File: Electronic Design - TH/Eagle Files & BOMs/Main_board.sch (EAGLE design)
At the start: 46 parts, among them IC2 ATMEGA328-PU, Q1 BSS192P, Q2 FQD7P20, X1 16MHz

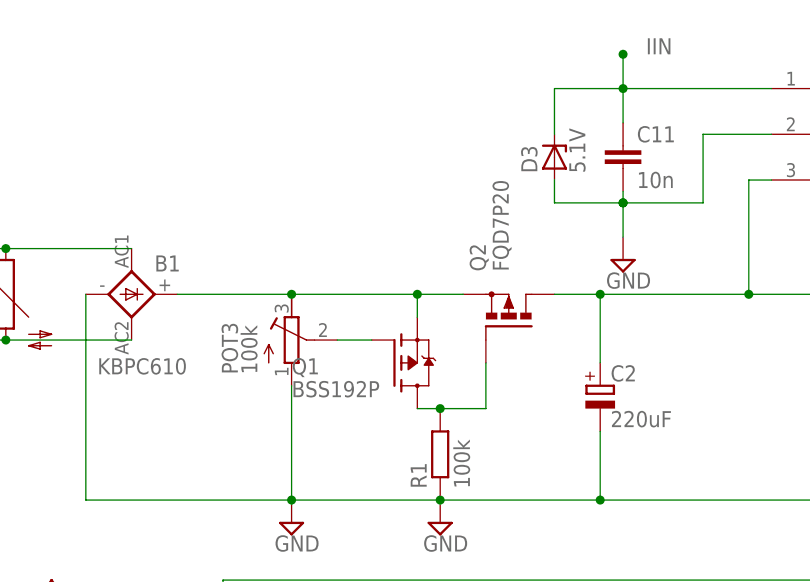
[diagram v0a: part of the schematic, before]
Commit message: replaced SMD resistors, caps and MOSFETs with TH components
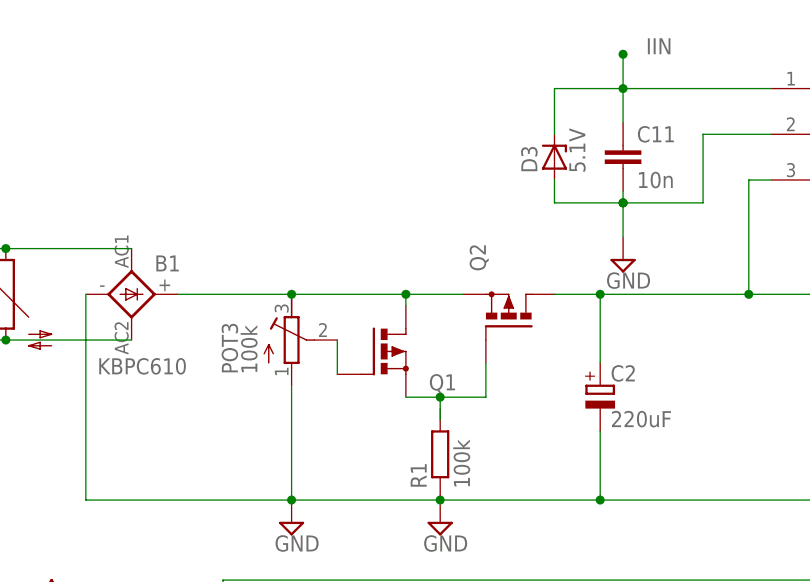
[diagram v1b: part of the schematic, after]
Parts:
- C1, C10, C11, C4, C5, C6, C7: device resistor:C-EUC1206K -> resistor:C-EU050-024X044
- C8, C9: device resistor:C-EUC0805K -> resistor:C-EU050-024X044
- PWR, UC_PWR: device adafruit:LEDSMT1206 -> led:LED3MM
- Q1: value BSS192P -> (none); device Samson:BSS192P -> Samson:PMOSFET_PTO220BH
- Q2: value FQD7P20 -> (none); device Samson:FQD7P20 -> Samson:PMOSFET_PTO220BH
- R10, R9: device resistor:R-EU_R0805 -> resistor:R-EU_0207/10
- R11, R12, R4, R5, R7, R8: device resistor:R-EU_R1206 -> resistor:R-EU_0207/10
- R2: device resistor:R-EU_M1206 -> resistor:R-EU_0207/15
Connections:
- net Q2_GATE: now also Q1.S; no longer Q1.D, R1.2
- net VIN_UNPROTECTED: now also Q1.D; no longer Q1.S
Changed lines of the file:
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@@
 <parts>
 <part name="B1" library="rectifier" deviceset="GBPC6" device="" value="KBPC610"/>
-<part name="C1" library="resistor" deviceset="C-EU" device="C1206K" value="10n"/>
+<part name="C1" library="resistor" deviceset="C-EU" device="050-024X044" value="10n"/>
 <part name="C2" library="resistor" deviceset="CPOL-EU" device="E3.5-10" value="220uF"/>
 <part name="POT3" library="resistor" deviceset="R-TRIMM" device="3296W" value="100k"/>
@@
 <part name="IC2" library="Arduino-AVR" deviceset="ATMEGA168-PU" device="" value="ATMEGA328-PU"/>
 <part name="X1" library="crystal" deviceset="CRYSTAL" device="HC49S" value="16MHz"/>
-<part name="R4" library="resistor" deviceset="R-EU_" device="R1206" value="10k"/>
+<part name="R4" library="resistor" deviceset="R-EU_" device="0207/10" value="10k"/>
 <part name="+5V1" library="supply1" deviceset="+5V" device=""/>
-<part name="C7" library="resistor" deviceset="C-EU" device="C1206K" value="0.1u"/>
-<part name="C9" library="resistor" deviceset="C-EU" device="C0805K" value="22p"/>
-<part name="C8" library="resistor" deviceset="C-EU" device="C0805K" value="22p"/>
+<part name="C7" library="resistor" deviceset="C-EU" device="050-024X044" value="0.1u"/>
+<part name="C9" library="resistor" deviceset="C-EU" device="050-024X044" value="22p"/>
+<part name="C8" library="resistor" deviceset="C-EU" device="050-024X044" value="22p"/>
 <part name="SUPPLY14" library="supply2" deviceset="GND" device=""/>
 <part name="SUPPLY17" library="supply2" deviceset="GND" device=""/>
@@
 <part name="S2" library="switch-omron" deviceset="10-XX" device=""/>
 <part name="+5V2" library="supply1" deviceset="+5V" device=""/>
-<part name="R5" library="resistor" deviceset="R-EU_" device="R1206" value="10k"/>
+<part name="R5" library="resistor" deviceset="R-EU_" device="0207/10" value="10k"/>
 <part name="SUPPLY3" library="supply2" deviceset="GND" device=""/>
 <part name="+5V3" library="supply1" deviceset="+5V" device=""/>
@@
 <part name="+3V1" library="supply1" deviceset="+5V" device=""/>
 <part name="VOUT" library="pinhead" deviceset="PINHD-1X3" device=""/>
-<part name="C6" library="resistor" deviceset="C-EU" device="C1206K" value="0.1u"/>
-<part name="C10" library="resistor" deviceset="C-EU" device="C1206K" value="0.1u"/>
+<part name="C6" library="resistor" deviceset="C-EU" device="050-024X044" value="0.1u"/>
+<part name="C10" library="resistor" deviceset="C-EU" device="050-024X044" value="0.1u"/>
 <part name="AIO" library="pinhead" deviceset="PINHD-1X6" device=""/>
 <part name="+5V4" library="supply1" deviceset="+5V" device=""/>
-<part name="R2" library="resistor" deviceset="R-EU_" device="M1206" value="0R01"/>
+<part name="R2" library="resistor" deviceset="R-EU_" device="0207/15" value="0R01"/>
 <part name="+3V2" library="supply1" deviceset="+5V" device=""/>
 <part name="SUPPLY1" library="supply2" deviceset="GND" device=""/>
 <part name="SUPPLY8" library="supply2" deviceset="GND" device=""/>
-<part name="R7" library="resistor" deviceset="R-EU_" device="R1206" value="1k"/>
-<part name="R8" library="resistor" deviceset="R-EU_" device="R1206" value="3k"/>
+<part name="R7" library="resistor" deviceset="R-EU_" device="0207/10" value="1k"/>
+<part name="R8" library="resistor" deviceset="R-EU_" device="0207/10" value="3k"/>
 <part name="U$1" library="Samson" deviceset="LM317" device=""/>
 <part name="U$2" library="Samson" deviceset="CS30" device=""/>
-<part name="C4" library="resistor" deviceset="C-EU" device="C1206K" value="0.1u"/>
-<part name="C5" library="resistor" deviceset="C-EU" device="C1206K" value="0.1u"/>
+<part name="C4" library="resistor" deviceset="C-EU" device="050-024X044" value="0.1u"/>
+<part name="C5" library="resistor" deviceset="C-EU" device="050-024X044" value="0.1u"/>
 <part name="SUPPLY10" library="supply2" deviceset="GND" device=""/>
 <part name="SUPPLY11" library="supply2" deviceset="GND" device=""/>
-<part name="C11" library="resistor" deviceset="C-EU" device="C1206K" value="10n"/>
+<part name="C11" library="resistor" deviceset="C-EU" device="050-024X044" value="10n"/>
 <part name="D3" library="diode" deviceset="ZPD" device="" value="5.1V"/>
-<part name="R9" library="resistor" deviceset="R-EU_" device="R0805" value="21k5"/>
-<part name="R10" library="resistor" deviceset="R-EU_" device="R0805" value="1k13"/>
+<part name="R9" library="resistor" deviceset="R-EU_" device="0207/10" value="21k5"/>
+<part name="R10" library="resistor" deviceset="R-EU_" device="0207/10" value="1k13"/>
 <part name="SUPPLY12" library="supply2" deviceset="GND" device=""/>
 <part name="D4" library="diode" deviceset="ZPD" device="" value="5.1V"/>
 <part name="SUPPLY13" library="supply2" deviceset="GND" device=""/>
 <part name="D5" library="diode" deviceset="ZPD" device="" value="5.1V"/>
-<part name="UC_PWR" library="adafruit" deviceset="LED" device="SMT1206"/>
-<part name="PWR" library="adafruit" deviceset="LED" device="SMT1206"/>
-<part name="R11" library="resistor" deviceset="R-EU_" device="R1206" value="2k"/>
-<part name="R12" library="resistor" deviceset="R-EU_" device="R1206" value="2k"/>
+<part name="UC_PWR" library="led" deviceset="LED" device="3MM"/>
+<part name="PWR" library="led" deviceset="LED" device="3MM"/>
+<part name="R11" library="resistor" deviceset="R-EU_" device="0207/10" value="2k"/>
+<part name="R12" library="resistor" deviceset="R-EU_" device="0207/10" value="2k"/>
 <part name="SUPPLY15" library="supply2" deviceset="GND" device=""/>
-<part name="Q1" library="Samson" deviceset="BSS192P" device=""/>
-<part name="Q2" library="Samson" deviceset="FQD7P20" device=""/>
+<part name="Q1" library="Samson" deviceset="PMOSFET_P" device="TO220BH"/>
+<part name="Q2" library="Samson" deviceset="PMOSFET_P" device="TO220BH"/>
 <part name="F2" library="fuse" deviceset="FUSE" device="SH22,5A" value="FUSESH22,5A"/>
 <part name="C12" library="resistor" deviceset="CPOL-EU" device="E3.5-8" value="100uF"/>
@@
 <instance part="R12" gate="G$1" x="138.43" y="33.02" rot="R90"/>
 <instance part="SUPPLY15" gate="GND" x="138.43" y="24.13"/>
-<instance part="Q1" gate="G$1" x="-52.07" y="81.28" rot="MR180"/>
+<instance part="Q1" gate="G$1" x="-55.88" y="82.55" rot="MR180"/>
 <instance part="Q2" gate="G$1" x="-41.91" y="86.36" rot="R90"/>
 <instance part="F2" gate="G$1" x="-111.76" y="93.98" smashed="yes">
@@
 <net name="VIN_UNPROTECTED" class="0">
 <segment>
-<wire x1="-52.07" y1="86.36" x2="-52.07" y2="88.9" width="0.1524" layer="91"/>
-<wire x1="-52.07" y1="88.9" x2="-46.99" y2="88.9" width="0.1524" layer="91"/>
 <pinref part="POT3" gate="G$1" pin="E"/>
-<wire x1="-66.04" y1="88.9" x2="-52.07" y2="88.9" width="0.1524" layer="91"/>
-<junction x="-52.07" y="88.9"/>
+<wire x1="-66.04" y1="88.9" x2="-53.34" y2="88.9" width="0.1524" layer="91"/>
 <pinref part="B1" gate="1" pin="+"/>
+<wire x1="-53.34" y1="88.9" x2="-46.99" y2="88.9" width="0.1524" layer="91"/>
 <wire x1="-78.74" y1="88.9" x2="-66.04" y2="88.9" width="0.1524" layer="91"/>
 <junction x="-66.04" y="88.9"/>
+<pinref part="Q2" gate="G$1" pin="S"/>
+<pinref part="Q1" gate="G$1" pin="D"/>
+<wire x1="-53.34" y1="87.63" x2="-53.34" y2="88.9" width="0.1524" layer="91"/>
+<junction x="-53.34" y="88.9"/>
+</segment>
+</net>
+<net name="Q2_GATE" class="0">
+<segment>
+<pinref part="Q2" gate="G$1" pin="G"/>
 <pinref part="Q1" gate="G$1" pin="S"/>
-<pinref part="Q2" gate="G$1" pin="S"/>
-</segment>
-</net>
-<net name="Q2_GATE" class="0">
-<segment>
-<pinref part="R1" gate="G$1" pin="2"/>
-<wire x1="-52.07" y1="76.2" x2="-49.53" y2="76.2" width="0.1524" layer="91"/>
-<wire x1="-49.53" y1="76.2" x2="-44.45" y2="76.2" width="0.1524" layer="91"/>
-<wire x1="-44.45" y1="76.2" x2="-44.45" y2="81.28" width="0.1524" layer="91"/>
-<junction x="-49.53" y="76.2"/>
-<pinref part="Q1" gate="G$1" pin="D"/>
-<pinref part="Q2" gate="G$1" pin="G"/>
+<wire x1="-44.45" y1="77.47" x2="-44.45" y2="81.28" width="0.1524" layer="91"/>
+<wire x1="-53.34" y1="77.47" x2="-49.53" y2="77.47" width="0.1524" layer="91"/>
+<wire x1="-49.53" y1="74.93" x2="-49.53" y2="77.47" width="0.1524" layer="91"/>
+<wire x1="-49.53" y1="77.47" x2="-44.45" y2="77.47" width="0.1524" layer="91"/>
+<junction x="-49.53" y="77.47"/>
 </segment>
 </net>
@@
 <segment>
 <pinref part="POT3" gate="G$1" pin="S"/>
-<wire x1="-57.15" y1="83.82" x2="-60.96" y2="83.82" width="0.1524" layer="91"/>
+<wire x1="-60.96" y1="80.01" x2="-60.96" y2="83.82" width="0.1524" layer="91"/>
 <pinref part="Q1" gate="G$1" pin="G"/>
 </segment>

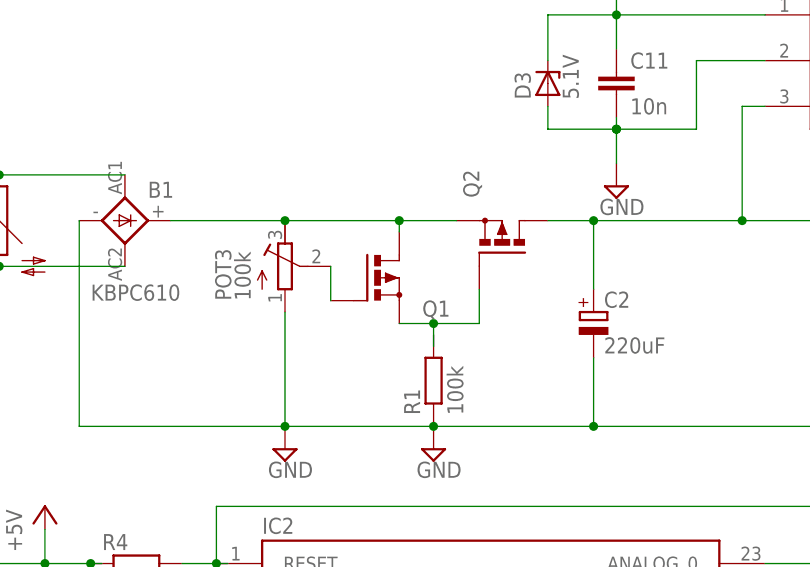
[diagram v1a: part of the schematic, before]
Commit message: correcting mosfet postion
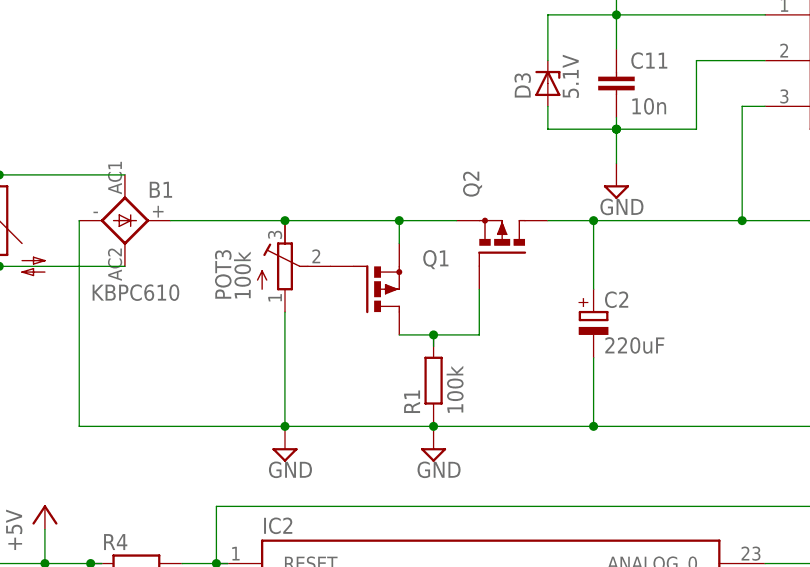
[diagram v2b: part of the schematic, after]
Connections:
- net Q2_GATE: now also Q1.D, R1.2; no longer Q1.S
- net VIN_UNPROTECTED: now also Q1.S; no longer Q1.D
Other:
- moved on the sheet: Q1
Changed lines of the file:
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@@
 <instance part="R12" gate="G$1" x="138.43" y="33.02" rot="R90"/>
 <instance part="SUPPLY15" gate="GND" x="138.43" y="24.13"/>
-<instance part="Q1" gate="G$1" x="-55.88" y="82.55" rot="MR180"/>
+<instance part="Q1" gate="G$1" x="-55.88" y="81.28"/>
 <instance part="Q2" gate="G$1" x="-41.91" y="86.36" rot="R90"/>
 <instance part="F2" gate="G$1" x="-111.76" y="93.98" smashed="yes">
@@
 <junction x="-66.04" y="88.9"/>
 <pinref part="Q2" gate="G$1" pin="S"/>
+<pinref part="Q1" gate="G$1" pin="S"/>
+<wire x1="-53.34" y1="86.36" x2="-53.34" y2="88.9" width="0.1524" layer="91"/>
+<junction x="-53.34" y="88.9"/>
+</segment>
+</net>
+<net name="Q2_GATE" class="0">
+<segment>
+<wire x1="-49.53" y1="74.93" x2="-49.53" y2="76.2" width="0.1524" layer="91"/>
 <pinref part="Q1" gate="G$1" pin="D"/>
-<wire x1="-53.34" y1="87.63" x2="-53.34" y2="88.9" width="0.1524" layer="91"/>
-<junction x="-53.34" y="88.9"/>
-</segment>
-</net>
-<net name="Q2_GATE" class="0">
-<segment>
+<wire x1="-53.34" y1="76.2" x2="-49.53" y2="76.2" width="0.1524" layer="91"/>
 <pinref part="Q2" gate="G$1" pin="G"/>
-<pinref part="Q1" gate="G$1" pin="S"/>
-<wire x1="-44.45" y1="77.47" x2="-44.45" y2="81.28" width="0.1524" layer="91"/>
-<wire x1="-53.34" y1="77.47" x2="-49.53" y2="77.47" width="0.1524" layer="91"/>
-<wire x1="-49.53" y1="74.93" x2="-49.53" y2="77.47" width="0.1524" layer="91"/>
-<wire x1="-49.53" y1="77.47" x2="-44.45" y2="77.47" width="0.1524" layer="91"/>
-<junction x="-49.53" y="77.47"/>
+<wire x1="-44.45" y1="76.2" x2="-44.45" y2="81.28" width="0.1524" layer="91"/>
+<wire x1="-44.45" y1="76.2" x2="-49.53" y2="76.2" width="0.1524" layer="91"/>
+<pinref part="R1" gate="G$1" pin="2"/>
+<junction x="-49.53" y="76.2"/>
 </segment>
 </net>
@@
 <segment>
 <pinref part="POT3" gate="G$1" pin="S"/>
-<wire x1="-60.96" y1="80.01" x2="-60.96" y2="83.82" width="0.1524" layer="91"/>
 <pinref part="Q1" gate="G$1" pin="G"/>
 </segment>
